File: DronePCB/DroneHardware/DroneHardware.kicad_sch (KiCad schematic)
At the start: 21 parts, among them SW1 SW_SPDT, U1 STM32F401RCT6, Y1 16MHz

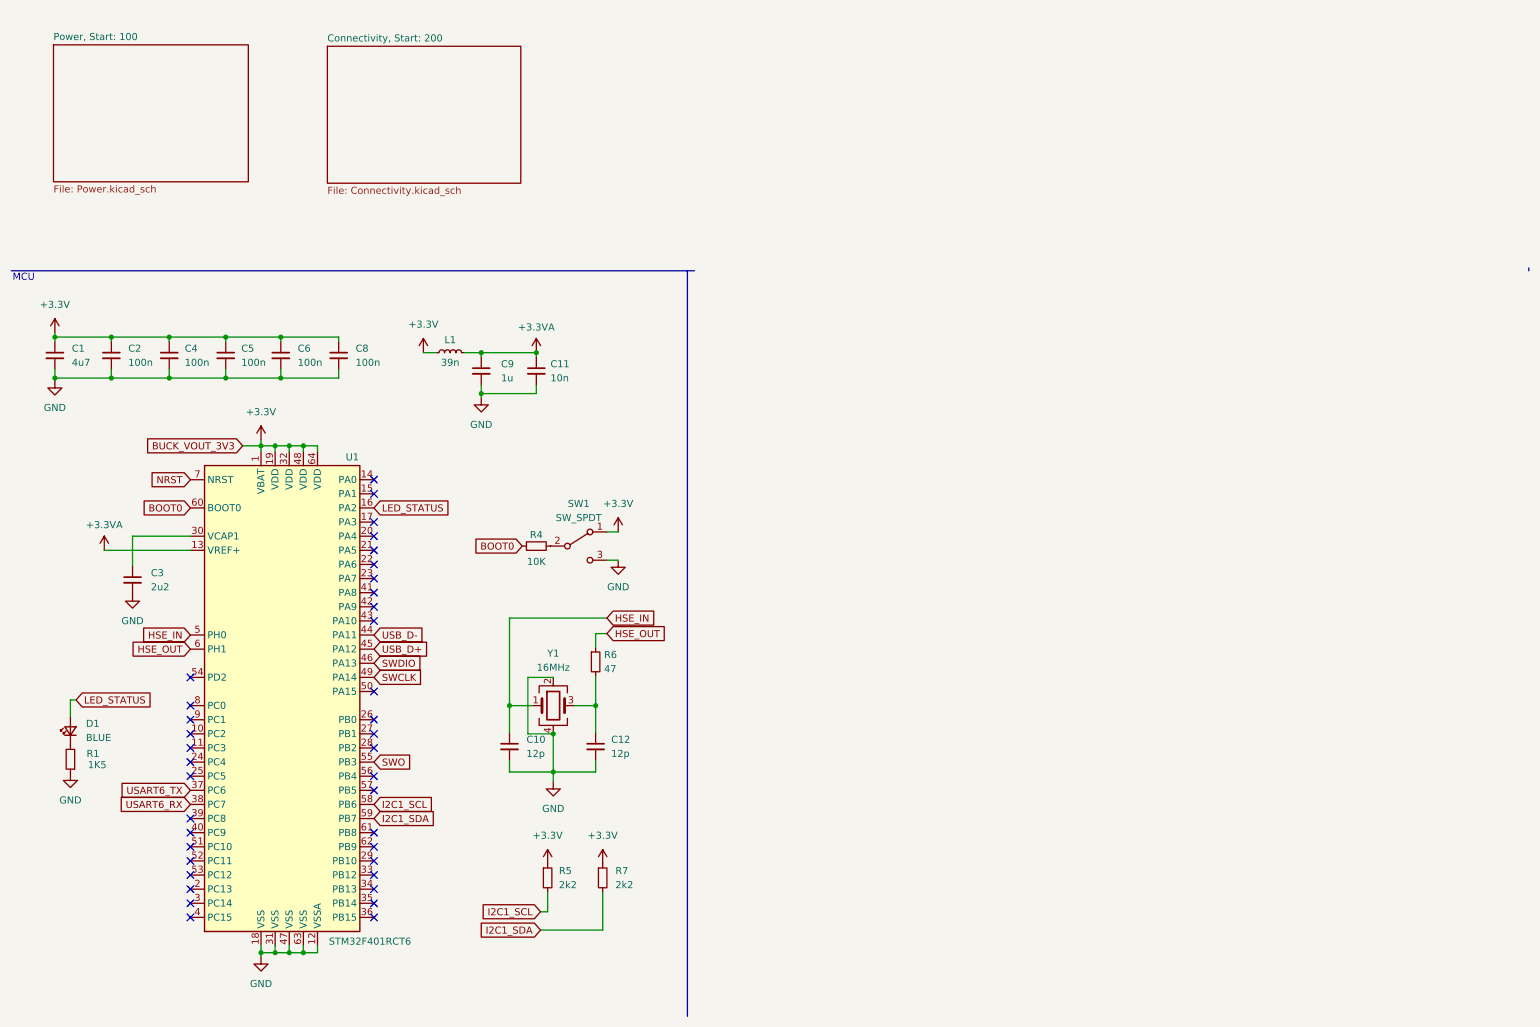
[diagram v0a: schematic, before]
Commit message: Inizio collegamenti MPU-6000
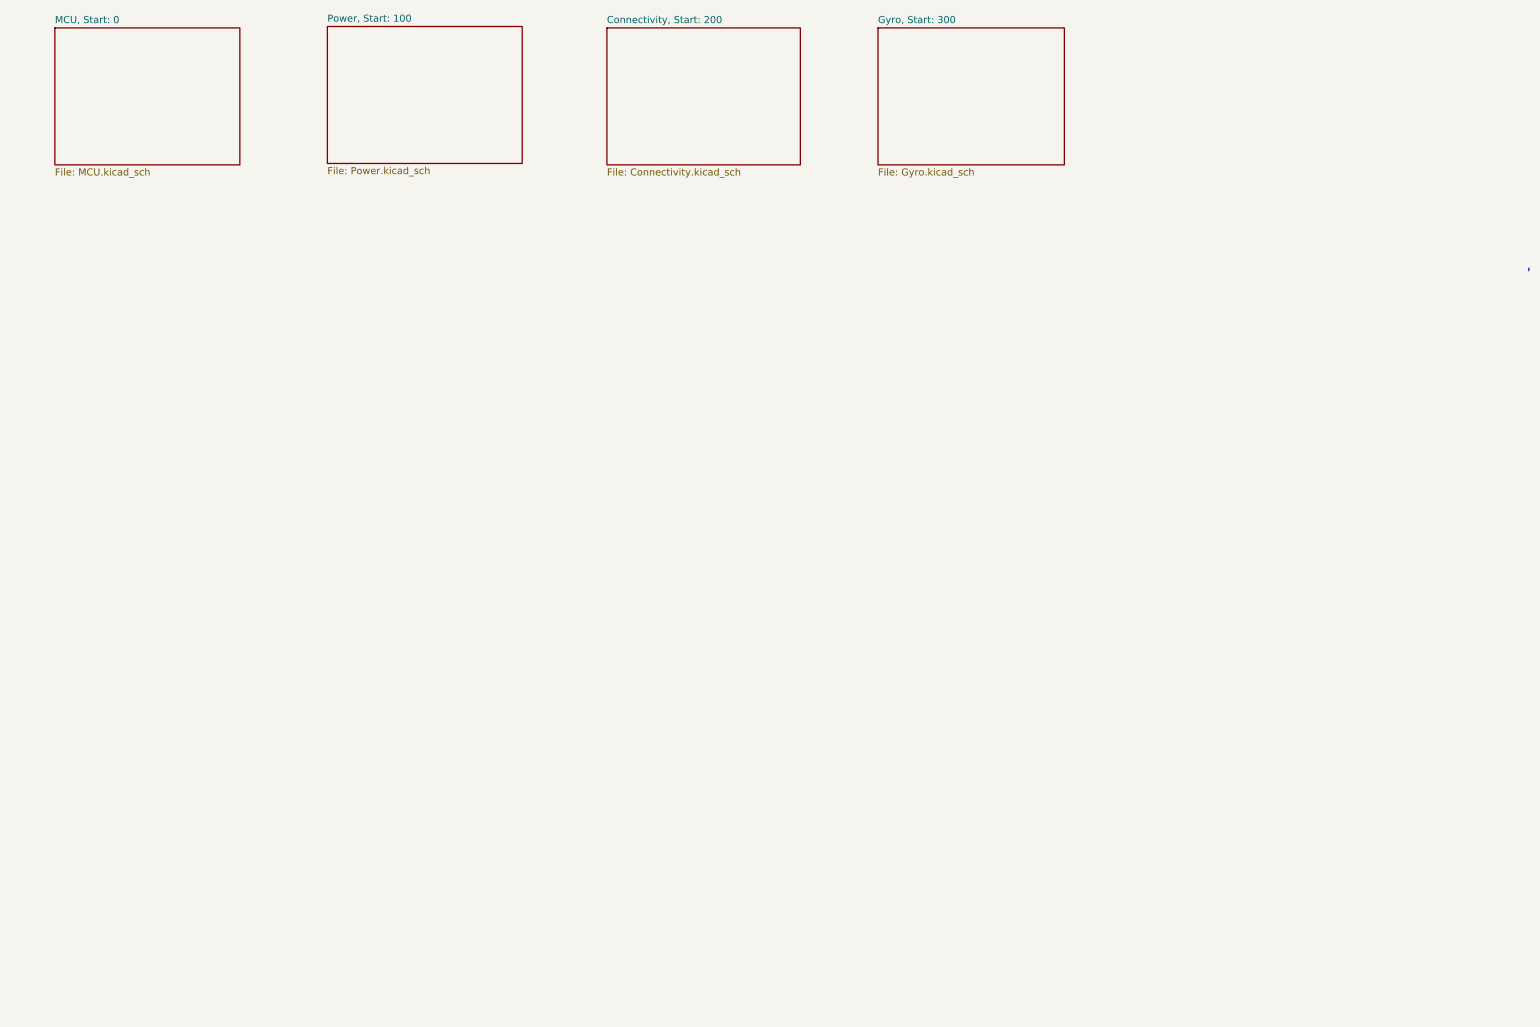
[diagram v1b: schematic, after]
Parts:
- removed C1: 4u7, Capacitor_SMD:C_0603_1608Metric, symbol Device:C_Small
- removed C10, C12: 12p, Capacitor_SMD:C_0402_1005Metric, symbol Device:C_Small
- removed C11: 10n, Capacitor_SMD:C_0402_1005Metric, symbol Device:C_Small
- removed C2, C4, C5, C6, C8: 100n, Capacitor_SMD:C_0402_1005Metric, symbol Device:C_Small
- removed C3: 2u2, Capacitor_SMD:C_0603_1608Metric, symbol Device:C_Small
- removed C9: 1u, Capacitor_SMD:C_0402_1005Metric, symbol Device:C_Small
- removed D1: BLUE, LED_SMD:LED_0603_1608Metric, symbol Device:LED_Small
- removed L1: 39n, Inductor_SMD:L_0402_1005Metric, symbol Device:L_Small
- removed R1: 1K5, Resistor_SMD:R_0603_1608Metric, symbol Device:R_Small
- removed R4: 10K, Resistor_SMD:R_0402_1005Metric, symbol Device:R_Small
- removed R5, R7: 2k2, Resistor_SMD:R_0603_1608Metric, symbol Device:R_Small
- removed R6: 47, Resistor_SMD:R_0402_1005Metric, symbol Device:R_Small
- removed SW1: SW_SPDT, Button_Switch_SMD:SW_SPDT_PCM12, symbol Switch:SW_SPDT
- removed U1: STM32F401RCT6, Package_QFP:LQFP-64_10x10mm_P0.5mm, symbol MCU_ST_STM32F4:STM32F401RCTx
- removed Y1: 16MHz, Crystal:Crystal_SMD_3225-4Pin_3.2x2.5mm, symbol Device:Crystal_GND24
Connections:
- no-connect marks 38 -> 0
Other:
- added sheet Gyro, Start: 300 (Gyro.kicad_sch)
- added sheet MCU, Start: 0 (MCU.kicad_sch)
- note removed: "MCU"

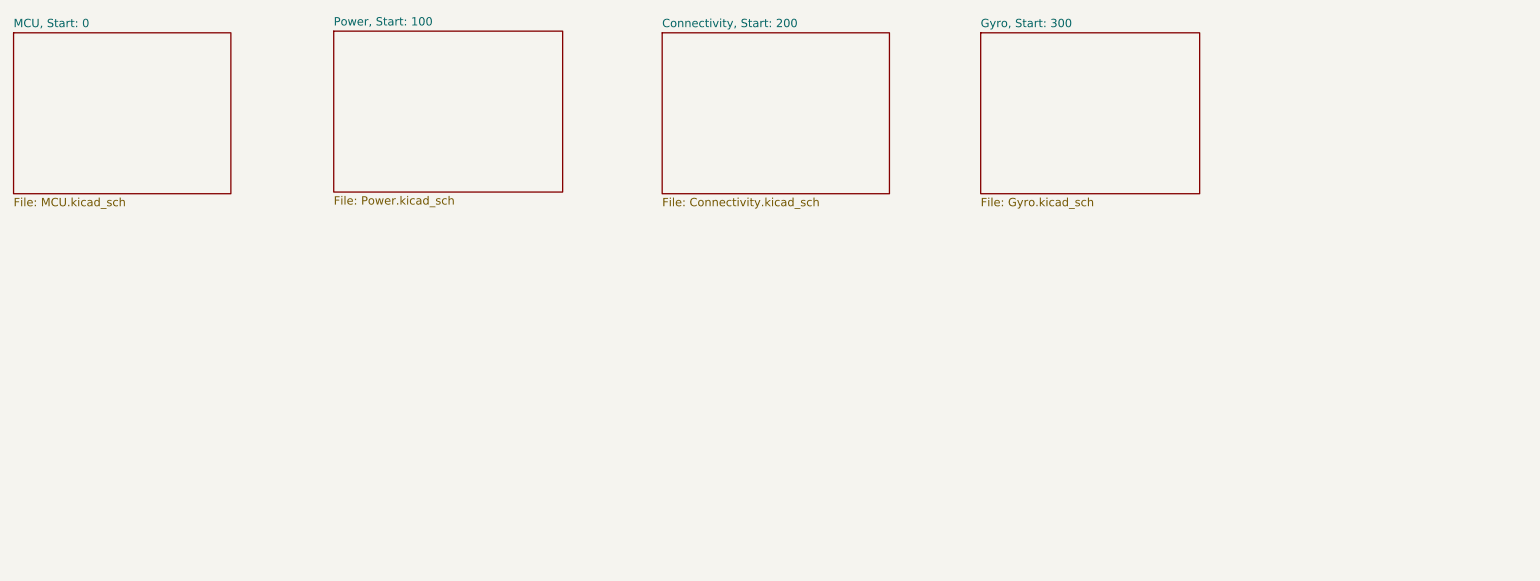
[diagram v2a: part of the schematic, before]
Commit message: Creazione PCB e utilizzo di processore STM32F405
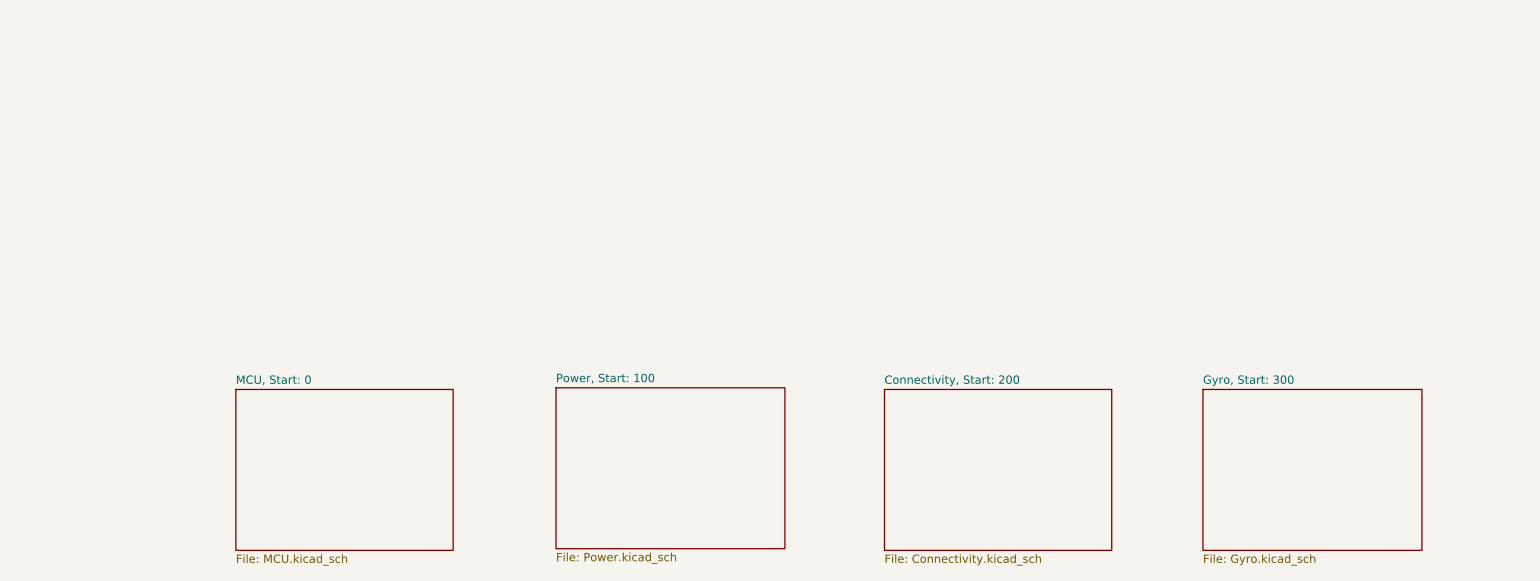
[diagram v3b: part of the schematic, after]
